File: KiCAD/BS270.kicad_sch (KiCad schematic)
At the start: 9 parts

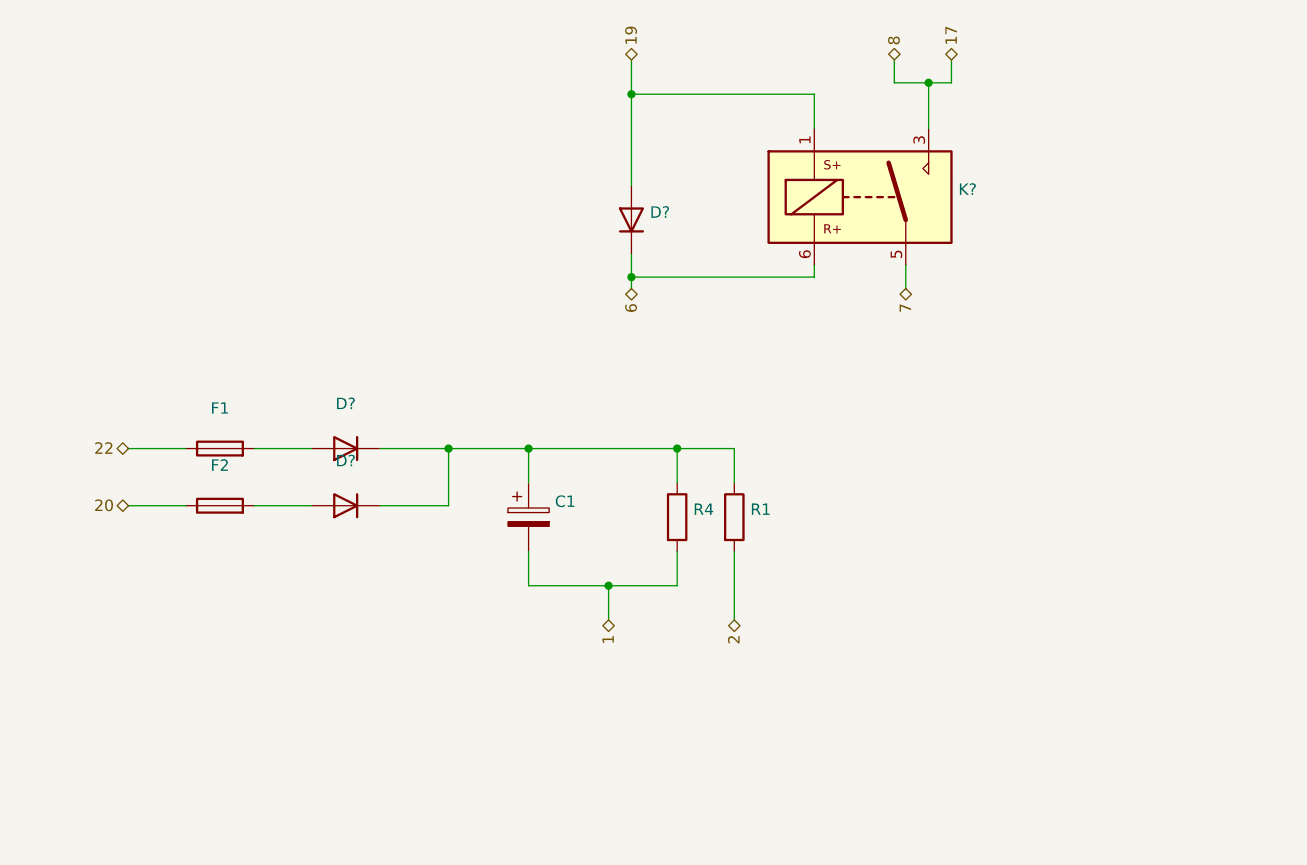
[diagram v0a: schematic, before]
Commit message: Schematics for BS112, BS230 and BS263 added
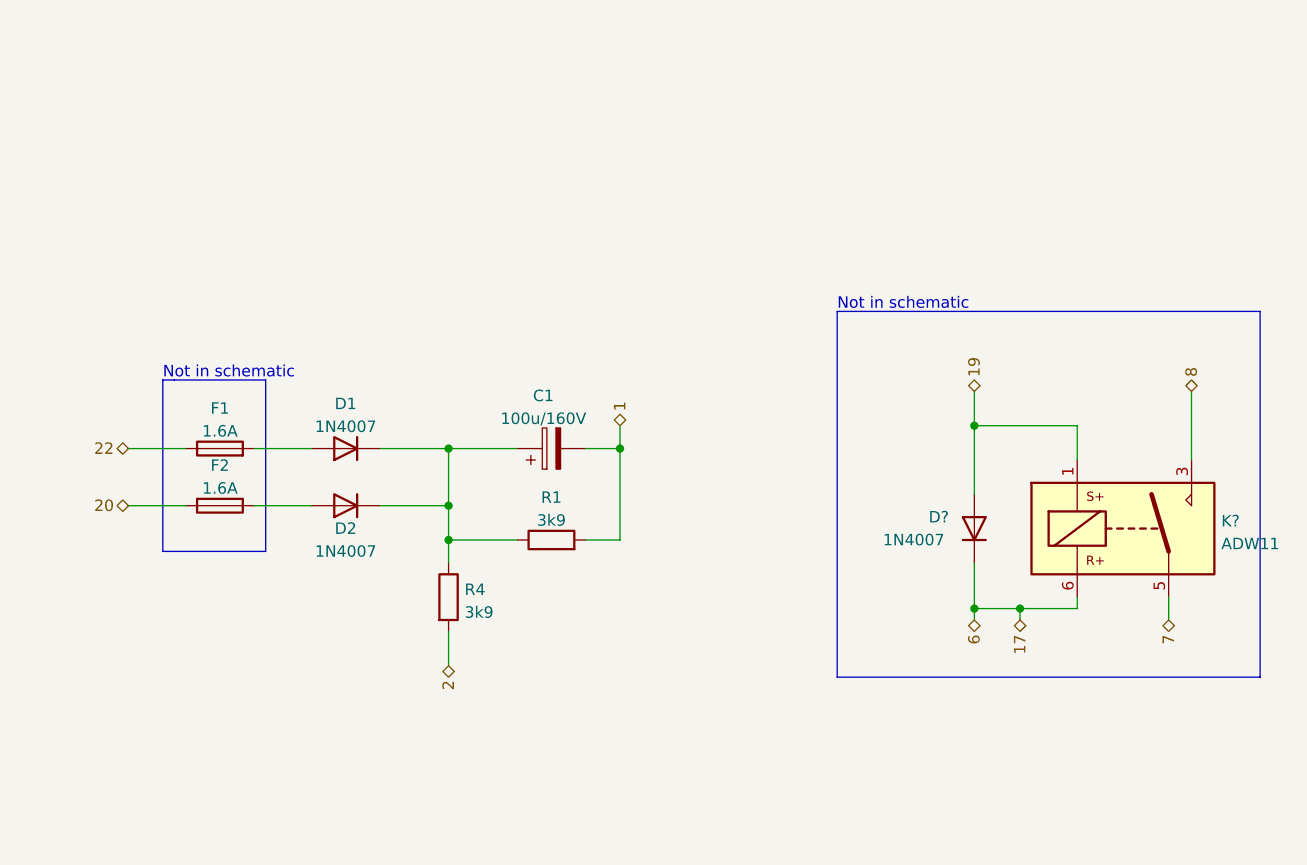
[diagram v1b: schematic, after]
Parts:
- C1: value (none) -> 100u/160V
- D1, D2: renamed from D?; value (none) -> 1N4007; footprint (none) -> Diode_THT:D_DO-41_SOD81_P10.16mm_Horizontal
- D?: value (none) -> 1N4007; footprint (none) -> Diode_THT:D_DO-41_SOD81_P10.16mm_Horizontal
- F1, F2: value (none) -> 1.6A
- K?: value (none) -> ADW11; footprint (none) -> Relay_THT:Relay_1P1T_NO_10x24x18.8mm_Panasonic_ADW11xxxxW_THT
- R1, R4: value (none) -> 3k9
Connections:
- net 6 is gone; now on net 17: D?.1 (K), K?.6
- net 1: now also R1.2; no longer R4.2
- net 17: no longer K?.3
- net 2: now also R4.2; no longer R1.2
- net 20: now also F2.2; no longer F2.1
- net at D2.2 (A): now also F2.1; no longer F2.2
- new net 8: K?.3
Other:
- note added: "Not in schematic"
- moved on the sheet: C1, D?, F2, K?, R1, R4

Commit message: Connections finished
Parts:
- D1, D2, D?: value 1N4007 -> (none)
- K?: value ADW11 -> (none)
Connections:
- net 1 renamed 1 0V
- net 17 renamed 17 K
- net 19 renamed 19 K
- net 2 renamed 2 TX Distr Scan
- net 20 renamed 20 64VAC
- net 22 renamed 22 64VAC
- net 7 renamed 7 KB
- net 8 renamed 8 KA
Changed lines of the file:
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@@
     (effects (font (size 1.27 1.27)) (justify left bottom))
   )
-  (hierarchical_label "2" (shape bidirectional) (at 105.41 116.84 270)
+  (hierarchical_label "2 TX Distr Scan" (shape output) (at 105.41 116.84 270)
     (effects (font (size 1.27 1.27)) (justify right))
   )
-  (hierarchical_label "19" (shape bidirectional) (at 163.83 86.36 90)
+  (hierarchical_label "19 K" (shape input) (at 163.83 86.36 90)
     (effects (font (size 1.27 1.27)) (justify left))
   )
-  (hierarchical_label "6" (shape bidirectional) (at 163.83 111.76 270)
+  (hierarchical_label "6 K" (shape input) (at 163.83 111.76 270)
     (effects (font (size 1.27 1.27)) (justify right))
   )
-  (hierarchical_label "22" (shape bidirectional) (at 69.85 92.71 180)
+  (hierarchical_label "22 64VAC" (shape input) (at 69.85 92.71 180)
     (effects (font (size 1.27 1.27)) (justify right))
   )
-  (hierarchical_label "17" (shape bidirectional) (at 168.91 111.76 270)
+  (hierarchical_label "17 K" (shape input) (at 168.91 111.76 270)
     (effects (font (size 1.27 1.27)) (justify right))
   )
-  (hierarchical_label "1" (shape bidirectional) (at 124.46 90.17 90)
+  (hierarchical_label "1 0V" (shape input) (at 124.46 90.17 90)
     (effects (font (size 1.27 1.27)) (justify left))
   )
-  (hierarchical_label "20" (shape bidirectional) (at 69.85 99.06 180)
+  (hierarchical_label "20 64VAC" (shape input) (at 69.85 99.06 180)
     (effects (font (size 1.27 1.27)) (justify right))
   )
-  (hierarchical_label "7" (shape bidirectional) (at 185.42 111.76 270)
+  (hierarchical_label "7 KB" (shape passive) (at 185.42 111.76 270)
     (effects (font (size 1.27 1.27)) (justify right))
   )
-  (hierarchical_label "8" (shape bidirectional) (at 187.96 86.36 90)
+  (hierarchical_label "8 KA" (shape passive) (at 187.96 86.36 90)
     (effects (font (size 1.27 1.27)) (justify left))
   )
   (symbol (lib_id "Diode:1N4007") (at 93.98 99.06 180) (unit 1)
     (in_bom yes) (on_board yes)
-    (property "Reference" "D?" (id 0) (at 93.98 101.6 0))
-    (property "Value" "1N4007" (id 1) (at 93.98 104.14 0))
+    (property "Reference" "D2" (id 0) (at 93.98 101.6 0))
+    (property "Value" "" (id 1) (at 93.98 104.14 0))
     (property "Footprint" "Diode_THT:D_DO-41_SOD81_P10.16mm_Horizontal" (id 2) (at 93.98 94.615 0)
       (effects (font (size 1.27 1.27)) hide)
@@
   (symbol (lib_id "Diode:1N4007") (at 93.98 92.71 180) (unit 1)
     (in_bom yes) (on_board yes) (fields_autoplaced)
-    (property "Reference" "D?" (id 0) (at 93.98 87.7402 0))
-    (property "Value" "1N4007" (id 1) (at 93.98 90.2771 0))
+    (property "Reference" "D1" (id 0) (at 93.98 87.7402 0))
+    (property "Value" "" (id 1) (at 93.98 90.2771 0))
     (property "Footprint" "Diode_THT:D_DO-41_SOD81_P10.16mm_Horizontal" (id 2) (at 93.98 88.265 0)
       (effects (font (size 1.27 1.27)) hide)
@@
     (in_bom yes) (on_board yes)
     (property "Reference" "D?" (id 0) (at 158.75 100.33 90)
-      (effects (font (size 1.27 1.27)) (justify right))
+      (effects (font (size 1.27 1.27)) (justify right) hide)
     )
-    (property "Value" "1N4007" (id 1) (at 153.67 102.87 90)
-      (effects (font (size 1.27 1.27)) (justify right))
+    (property "Value" "" (id 1) (at 153.67 102.87 90)
+      (effects (font (size 1.27 1.27)) (justify right) hide)
     )
     (property "Footprint" "Diode_THT:D_DO-41_SOD81_P10.16mm_Horizontal" (id 2) (at 168.275 101.6 0)
@@
     (in_bom yes) (on_board yes) (fields_autoplaced)
     (property "Reference" "K?" (id 0) (at 191.262 100.7653 0)
-      (effects (font (size 1.27 1.27)) (justify left))
+      (effects (font (size 1.27 1.27)) (justify left) hide)
     )
-    (property "Value" "ADW11" (id 1) (at 191.262 103.3022 0)
-      (effects (font (size 1.27 1.27)) (justify left))
+    (property "Value" "" (id 1) (at 191.262 102.0338 0)
+      (effects (font (size 1.27 1.27)) (justify left) hide)
     )
     (property "Footprint" "Relay_THT:Relay_1P1T_NO_10x24x18.8mm_Panasonic_ADW11xxxxW_THT" (id 2) (at 213.995 102.87 0)

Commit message: Labels
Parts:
- D1, D2: value (none) -> DD006
- D?: value (none) -> 1N4007
- K?: value (none) -> ADW11
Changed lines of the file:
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@@
     (in_bom yes) (on_board yes)
     (property "Reference" "D2" (id 0) (at 93.98 101.6 0))
-    (property "Value" "" (id 1) (at 93.98 104.14 0))
+    (property "Value" "DD006" (id 1) (at 93.98 104.14 0))
     (property "Footprint" "Diode_THT:D_DO-41_SOD81_P10.16mm_Horizontal" (id 2) (at 93.98 94.615 0)
       (effects (font (size 1.27 1.27)) hide)
@@
     (in_bom yes) (on_board yes) (fields_autoplaced)
     (property "Reference" "D1" (id 0) (at 93.98 87.7402 0))
-    (property "Value" "" (id 1) (at 93.98 90.2771 0))
+    (property "Value" "DD006" (id 1) (at 93.98 90.2771 0))
     (property "Footprint" "Diode_THT:D_DO-41_SOD81_P10.16mm_Horizontal" (id 2) (at 93.98 88.265 0)
       (effects (font (size 1.27 1.27)) hide)
@@
       (effects (font (size 1.27 1.27)) (justify right) hide)
     )
-    (property "Value" "" (id 1) (at 153.67 102.87 90)
+    (property "Value" "1N4007" (id 1) (at 153.67 102.87 90)
       (effects (font (size 1.27 1.27)) (justify right) hide)
     )
@@
       (effects (font (size 1.27 1.27)) (justify left) hide)
     )
-    (property "Value" "" (id 1) (at 191.262 102.0338 0)
+    (property "Value" "ADW11" (id 1) (at 191.262 102.0338 0)
       (effects (font (size 1.27 1.27)) (justify left) hide)
     )
